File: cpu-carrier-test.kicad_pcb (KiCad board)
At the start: 4 copper layers, 100 x 92 mm, 211 parts, among them J1 Micro_SD_Card_Det, J1101 USB_miniB, J1102 USB_C_Receptacle_USB2.0, J19 SFP, J20 SFP_CAGE, J2001 BNC, J2051 BNC, J2201 BEL_0845_2G1T_H5, J4 JTAG, J5 Molex_0936263508, J6 USB_A, SW1 SW_Push, SW2101 SW_DIP_x08, U1 TXS0108EPW, U1101 USB3740B-AI9, U1102 UTC2000, U1103 FT232RL, U1104 74LVC1G00, U1105 SC185, U2001 74LVC2T45DC, U2051 74LVC2T45DC, U2101 74LVC1G06, U2102 74LVC1G06, U2103 PCA9306, U2104 24AA0x, U2201 74LVC1G06, U2202 74LVC1G06, U2301 lan9254, U6 PCA9546AD, U8 74AC125, U9 TPS2051B, X2301 FNETHE025

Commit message: added more component values/part numbers
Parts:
- J5: value Molex_0936263508 -> GigE-RJ45

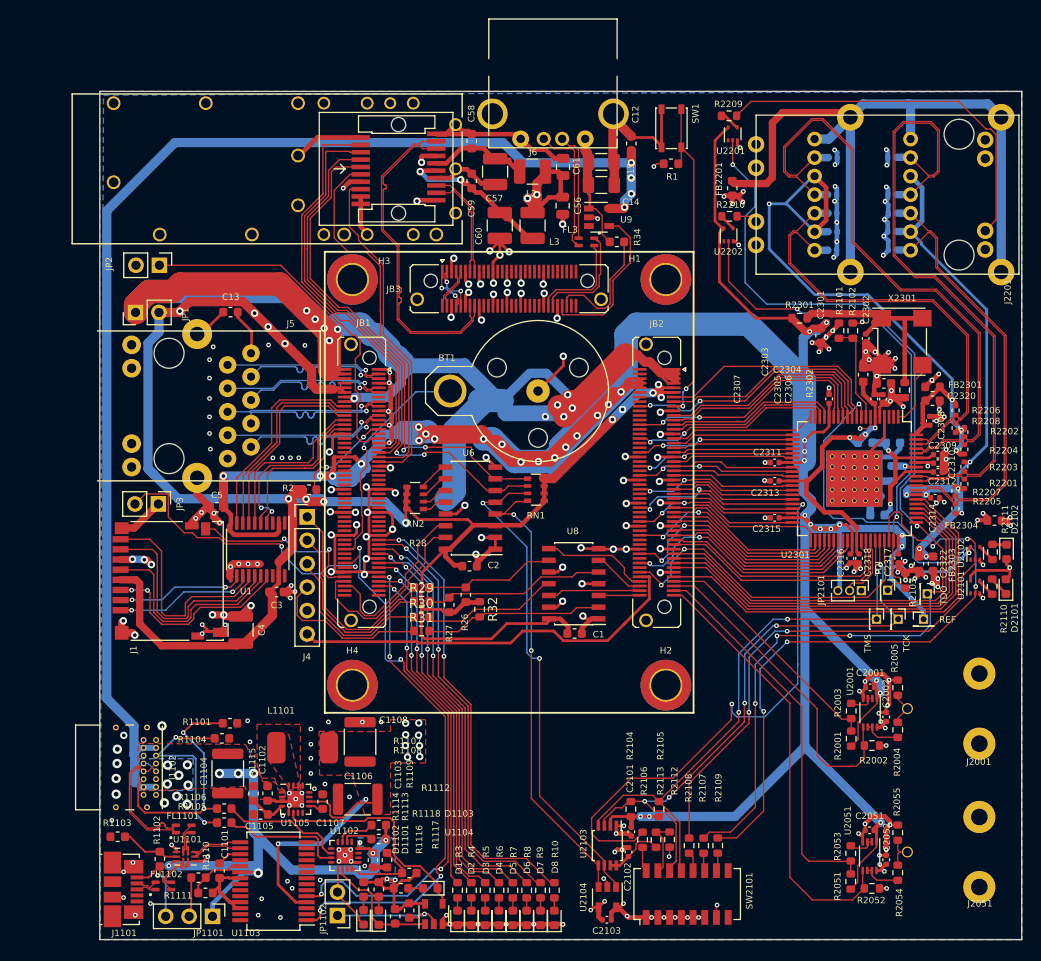
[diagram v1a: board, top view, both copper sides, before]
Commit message: re-routed usbA (proper diff-pair); added mounting holes
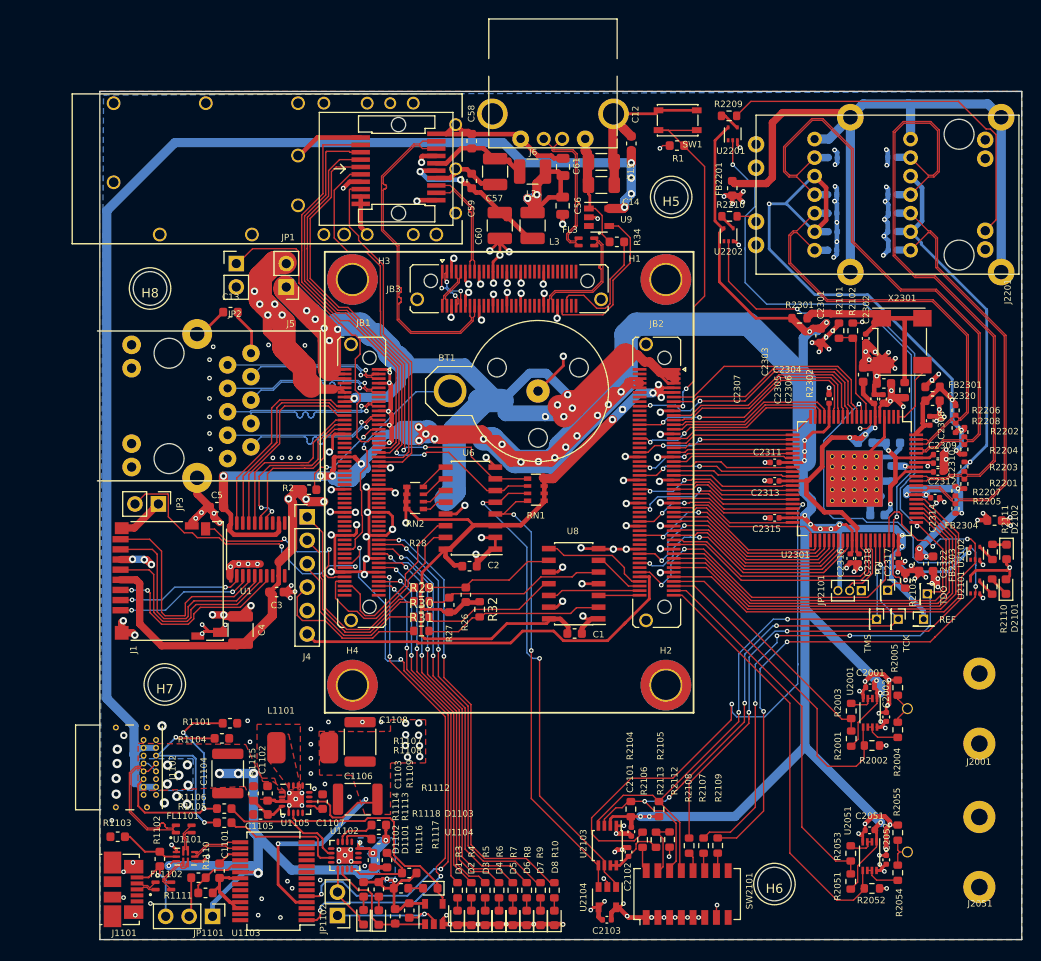
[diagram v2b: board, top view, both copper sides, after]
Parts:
- added H5: Foot, proj_footprints:foot_ff-13, F.Cu at (162.0, 41.5)
- added H6: Foot, proj_footprints:foot_ff-13, F.Cu at (173.2, 116.0)
- added H7: Foot, proj_footprints:foot_ff-13, F.Cu at (107.0, 94.3)
- added H8: Foot, proj_footprints:foot_ff-13, F.Cu at (105.5, 51.4)
- moved JP1 16.6 mm to (120.2, 51.2), turned to 180 degrees
- moved JP2 8.34 mm to (114.8, 48.7), turned to 0 degrees
- moved R1 2.08 mm to (162.6, 35.9)
- moved SW1 1.11 mm to (162.7, 33.1), turned to 0 degrees
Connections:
- net Net-(FL3-Pad2) renamed /USB, SDIO, RJ45, JTAG, UART, I2C/USBA_N
- net Net-(FL3-Pad3) renamed /USB, SDIO, RJ45, JTAG, UART, I2C/USBA_P
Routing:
- net +3V3_PWR_OUT: track 329.7 -> 279.8 mm
- net +3V3: track 267.7 -> 233.3 mm, vias 37 -> 38
- net /B2B Connector/MODE: track 39.0 -> 34.1 mm
- net /USB, SDIO, RJ45, JTAG, UART, I2C/USBA_N: track 11.9 -> 15.5 mm
- net /B2B Connector/RESIN: track 36.2 -> 38.8 mm
- net B35_L20_P: track 42.2 -> 40.5 mm
- net OTG_D_P: track 11.0 -> 12.6 mm
- net B35_L25: track 48.1 -> 46.7 mm
- net /USB, SDIO, RJ45, JTAG, UART, I2C/USBA_P: track 14.6 -> 15.5 mm
- net OTG_D_N: track 12.0 -> 12.6 mm

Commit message: use rj45/Gige + USB combo connector; hooked up LEDs
no more GND window under GigE diff-pairs on power-plane
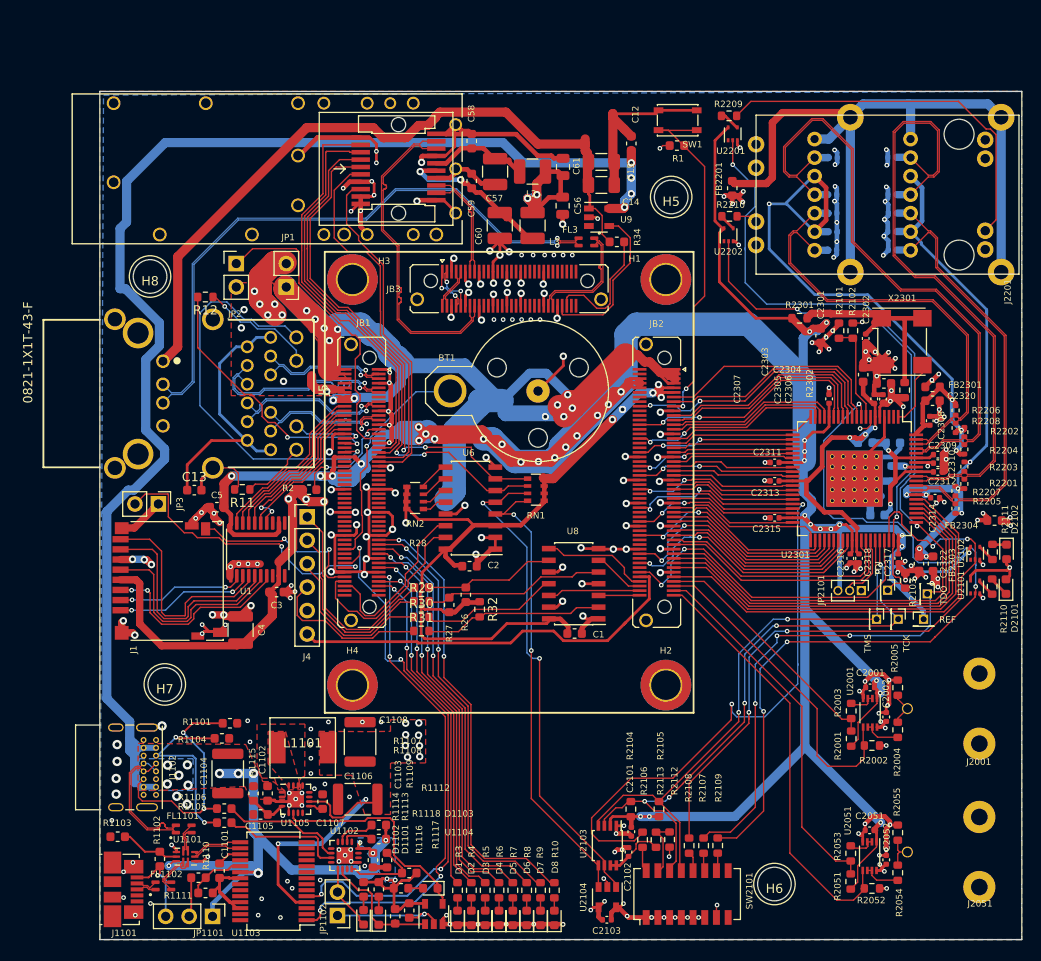
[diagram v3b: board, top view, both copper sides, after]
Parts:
- removed J6: USB_A, proj_footprints:USB_A_SS52100_001
- added R11: 100, Resistor_SMD:R_0603_1608Metric, F.Cu at (115.5, 73.2)
- added R12: 100, Resistor_SMD:R_0603_1608Metric, F.Cu at (111.5, 52.3)
- J5: value GigE-RJ45 -> 0821-1X1T-43-F; footprint proj_footprints:Molex_936263508 -> proj_footprints:BEL_0821-1X1T-43-F
- L1101: footprint proj_footprints:L_CDMC6D28 -> proj_footprints:L_TDK_SPM6530
- moved C13 19.7 mm to (110.2, 73.2), turned to 0 degrees
- moved J5 10.5 mm to (106.8, 62.8)
- moved H8 1.30 mm to (105.5, 50.1)
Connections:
- J5 pad 1: Net-(C13-Pad1) -> Net-(C14-Pad1)
- J5 pad 10: OTG_ID -> PHY_MDIO1_P
- J5 pad 11: Net-(J5-Pad11) -> PHY_MDIO1_N
- J5 pad 12: Net-(J5-Pad12) -> Net-(C13-Pad1)
- J5 pad 13: Net-(J5-Pad13) -> Net-(C13-Pad1)
- J5 pad 14: Net-(J5-Pad14) -> PHY_MDIO3_P
- J5 pad 2: PHY_MDIO0_P -> /USB, SDIO, RJ45, JTAG, UART, I2C/USBA_N
- J5 pad 3: PHY_MDIO0_N -> /USB, SDIO, RJ45, JTAG, UART, I2C/USBA_P
- J5 pad 4: PHY_MDIO1_P -> OTG_ID
- J5 pad 5: PHY_MDIO1_N -> OTG_ID
- J5 pad 6: PHY_MDIO2_P -> OTG_ID
- J5 pad 7: PHY_MDIO2_N -> Net-(C13-Pad1)
- J5 pad 8: PHY_MDIO3_P -> PHY_MDIO2_N
- J5 pad 9: PHY_MDIO3_N -> PHY_MDIO2_P
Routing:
- net Net-(C14-Pad1): track 12.4 -> 77.7 mm
- net /USB, SDIO, RJ45, JTAG, UART, I2C/USBA_P: track 15.5 -> 64.8 mm, vias 0 -> 1
- net /USB, SDIO, RJ45, JTAG, UART, I2C/USBA_N: track 15.5 -> 64.8 mm, vias 0 -> 1
- net B13_L5_N: track 0.00 -> 43.9 mm, vias 0 -> 1
- net B13_L3_N: track 0.00 -> 29.3 mm, vias 0 -> 2
- net Net-(C13-Pad1): track 5.19 -> 30.0 mm
- net +3V3: track 233.3 -> 210.4 mm, vias 38 -> 42
- net OTG_ID: track 420.5 -> 437.7 mm, vias 233 -> 236
- net Net-(J5-Pad21): track 0.00 -> 12.5 mm, vias 0 -> 1
- net B13_L3_P: track 0.00 -> 8.32 mm, vias 0 -> 1
- net Net-(J5-Pad19): track 0.00 -> 7.18 mm
- net +5V: track 218.3 -> 223.9 mm
- net +3V3_PWR_OUT: track 279.8 -> 284.9 mm, vias 21 -> 22
- net SD0_D2_MIO44: track 22.8 -> 18.1 mm
- net SD0_D1_MIO43: track 21.3 -> 17.4 mm
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- added copper zone on F.Cu, net +3V3
- removed copper zone on In2.Cu, net OTG_ID

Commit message: Several changes; converging to prototype version 1.0.0
Added header for connecting external power-supply (in case
chips are not available)
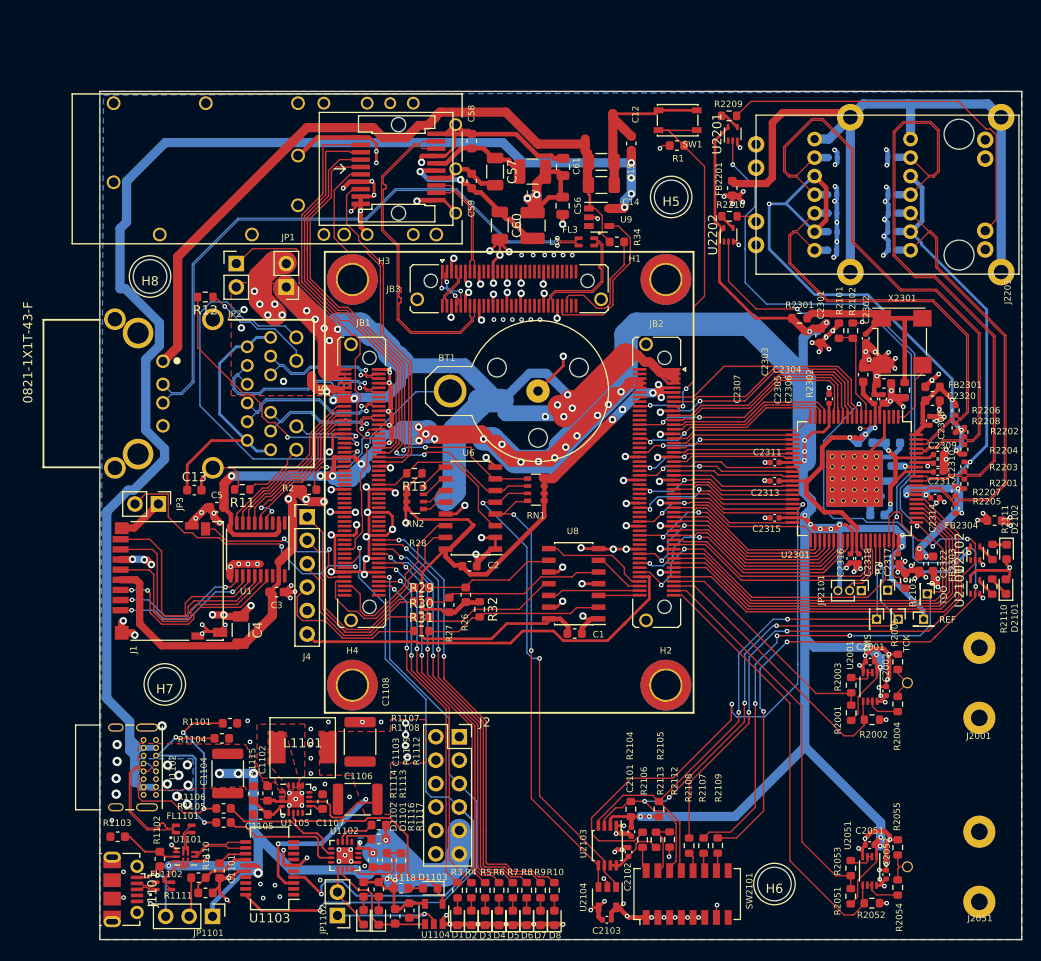
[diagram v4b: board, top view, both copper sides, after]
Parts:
- added J2: Pwr_fallback, Connector_PinSocket_2.54mm:PinSocket_2x06_P2.54mm_Vertical, F.Cu at (139.0, 100.0)
- added R13: 10k, Resistor_SMD:R_0603_1608Metric, F.Cu at (134.1, 71.4)
- C4, C57, C60: value 10uF_1210 -> 10u; footprint Capacitor_SMD:C_1210_3225Metric -> Capacitor_SMD:C_1206_3216Metric
- J1101: value USB_miniB -> USB_microB; footprint Connector_USB:USB_Micro-B_Molex_47346-0001 -> Connector_USB:USB_Micro-B_Molex-105017-0001
- R1113, R1114, R1118: value 1k5 -> 1k
- U1103: value FT232RL -> FT231XS; footprint Package_SO:SSOP-28_5.3x10.2mm_P0.65mm -> Package_SO:SSOP-20_3.9x8.7mm_P0.635mm
- U2101, U2102, U2201, U2202: footprint Package_TO_SOT_SMD:SOT-553 -> proj_footprints:SOT-5x3
- moved C2001 2.80 mm to (183.6, 91.8)
- moved U2001 2.80 mm to (183.6, 94.6)
- moved C2002 2.80 mm to (185.3, 95.0)
- moved J2001 2.80 mm to (195.4, 94.2)
- moved R2001 2.80 mm to (181.5, 97.4)
- moved R2002 2.80 mm to (183.8, 98.2)
- moved R2003 2.80 mm to (181.5, 94.4)
- moved R2004 2.80 mm to (186.6, 96.5)
- moved R2005 2.80 mm to (186.6, 91.9)
- moved R1112 1.63 mm to (132.7, 113.4), turned to 90 degrees
- moved C2052 1.60 mm to (185.3, 115.0)
- moved C2051 1.60 mm to (183.5, 111.8)
- moved J2051 1.60 mm to (195.4, 114.1)
- moved R2051 1.60 mm to (181.4, 117.3)
- moved R2052 1.60 mm to (183.8, 118.0)
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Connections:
- U1103 pad 1: UART_RX_MIO14 -> Net-(U1103-Pad1)
- U1103 pad 11: Net-(U1103-Pad11) -> /power-and-uart/Sheet5C4CE702/USB_P
- U1103 pad 12: Net-(U1103-Pad12) -> /power-and-uart/Sheet5C4CE702/USB_N
- U1103 pad 13: Net-(U1103-Pad13) -> Net-(C1101-Pad1)
- U1103 pad 14: Net-(U1103-Pad14) -> Net-(R1110-Pad2)
- U1103 pad 15: /power-and-uart/Sheet5C4CE702/USB_P -> +5V
- U1103 pad 16: /power-and-uart/Sheet5C4CE702/USB_N -> OTG_ID
- U1103 pad 17: Net-(C1101-Pad1) -> Net-(U1103-Pad17)
- U1103 pad 18: OTG_ID -> Net-(U1103-Pad18)
- U1103 pad 19: Net-(R1110-Pad2) -> Net-(U1103-Pad19)
- U1103 pad 20: +5V -> UART_RX_MIO14
- U1103 pad 3: Net-(U1103-Pad3) -> +3V3_PWR_OUT
- U1103 pad 4: +3V3_PWR_OUT -> UART_TX_MIO15
- U1103 pad 5: UART_TX_MIO15 -> Net-(U1103-Pad5)
- U1103 pad 6: Net-(U1103-Pad6) -> OTG_ID
- U1103 pad 7: OTG_ID -> Net-(U1103-Pad7)
- U1103 pad 8: (no net) -> Net-(U1103-Pad8)
- U6 pad 3: +3V3 -> B13_L8_N
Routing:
- net +5V: track 223.9 -> 245.3 mm
- net B13_L8_N: track 0.00 -> 18.0 mm
- net +3V3_PWR_OUT: track 284.9 -> 297.9 mm, vias 22 -> 18
- net UART_RX_MIO14: track 54.1 -> 64.7 mm, vias 4 -> 2
- net +3V3: track 210.4 -> 217.6 mm
- net UART_TX_MIO15: track 60.7 -> 67.2 mm, vias 4 -> 2
- net B35_L20_N: track 35.6 -> 30.5 mm
- net B35_L20_P: track 40.5 -> 42.1 mm
- net Net-(J1-Pad2): track 14.0 -> 15.5 mm
- net B35_L10_P: track 26.8 -> 25.7 mm
- net B35_L25: track 46.7 -> 47.9 mm
- net +1V8: track 410.7 -> 411.5 mm, vias 36 -> 37
- net Net-(R1110-Pad2): track 6.30 -> 7.13 mm
- net Net-(J1-Pad1): track 15.2 -> 16.0 mm
- net B13_L20_P: track 40.6 -> 39.9 mm
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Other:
- board text added: "EtherCat / Zynq Development Board V1.0.0"
